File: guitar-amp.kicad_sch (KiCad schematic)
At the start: 4 parts, among them J1 AudioJack2_SwitchT, U1 ECC81, U2 ECC81, U3 EL84

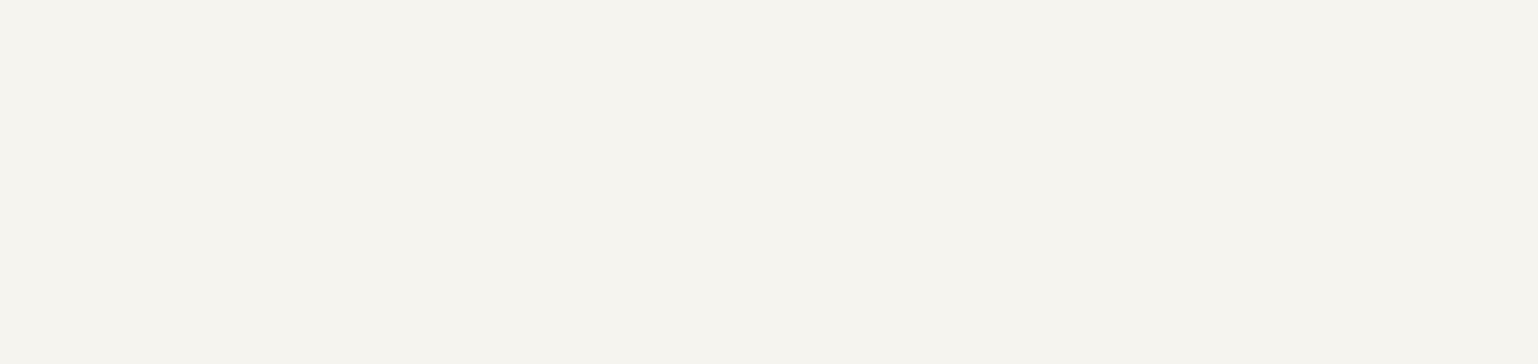
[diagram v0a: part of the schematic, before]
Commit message: Add resistors
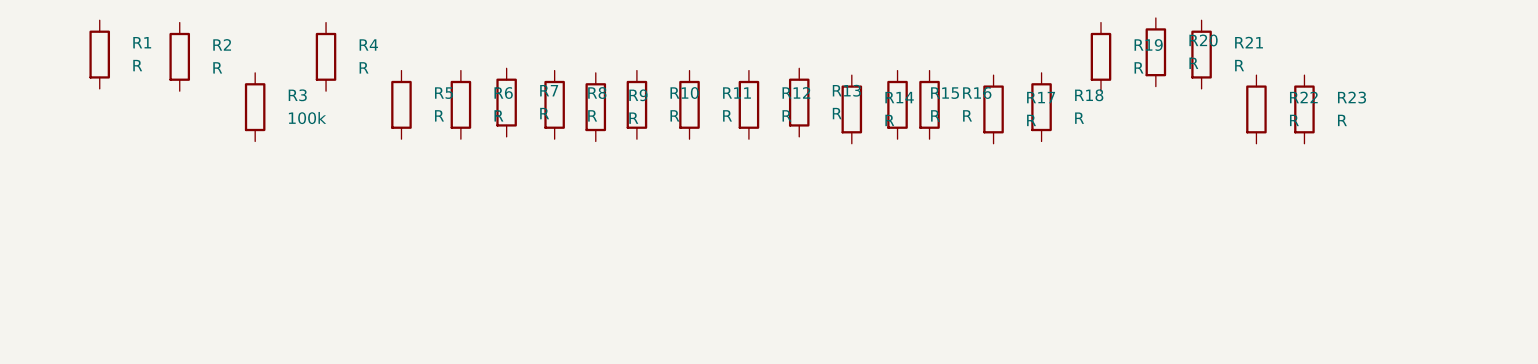
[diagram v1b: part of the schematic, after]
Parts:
- added R1, R19, R2, R20, R21, R4: R, Resistor_THT:R_Axial_DIN0411_L9.9mm_D3.6mm_P12.70mm_Horizontal, symbol Device:R
- added R10, R11, R12, R13, R14, R15, R16, R17, R18, R22, R23, R5, R6, R7, R8, R9: R, Resistor_THT:R_Axial_DIN0207_L6.3mm_D2.5mm_P7.62mm_Horizontal, symbol Device:R
- added R3: 100k, Resistor_THT:R_Axial_DIN0207_L6.3mm_D2.5mm_P7.62mm_Horizontal, symbol Device:R

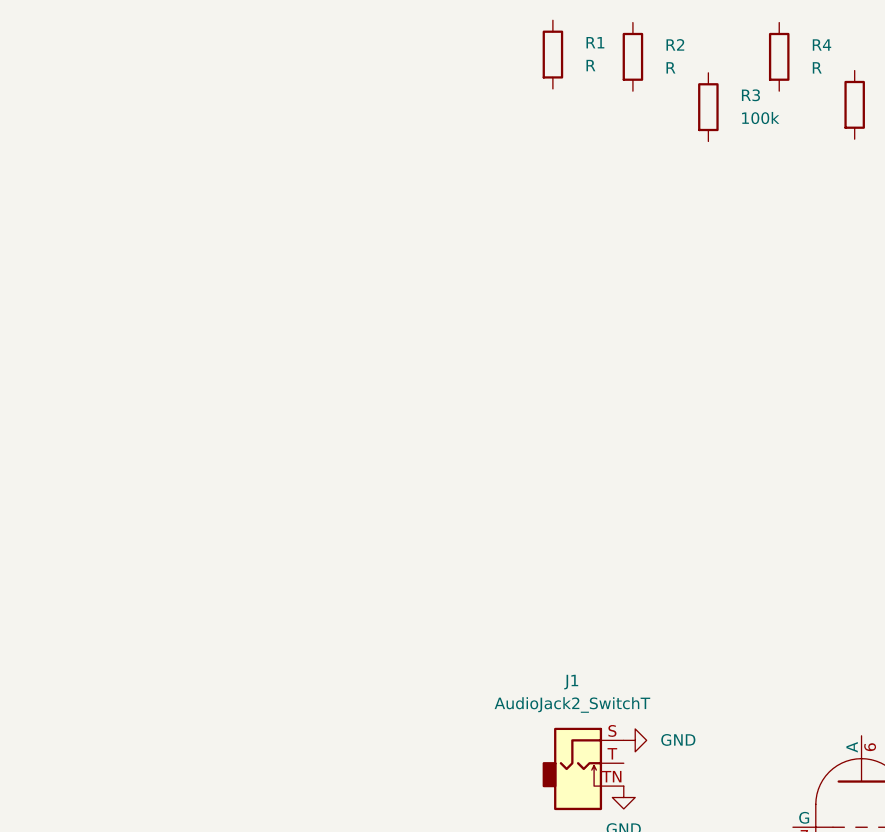
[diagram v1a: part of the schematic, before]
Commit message: Add capacitors
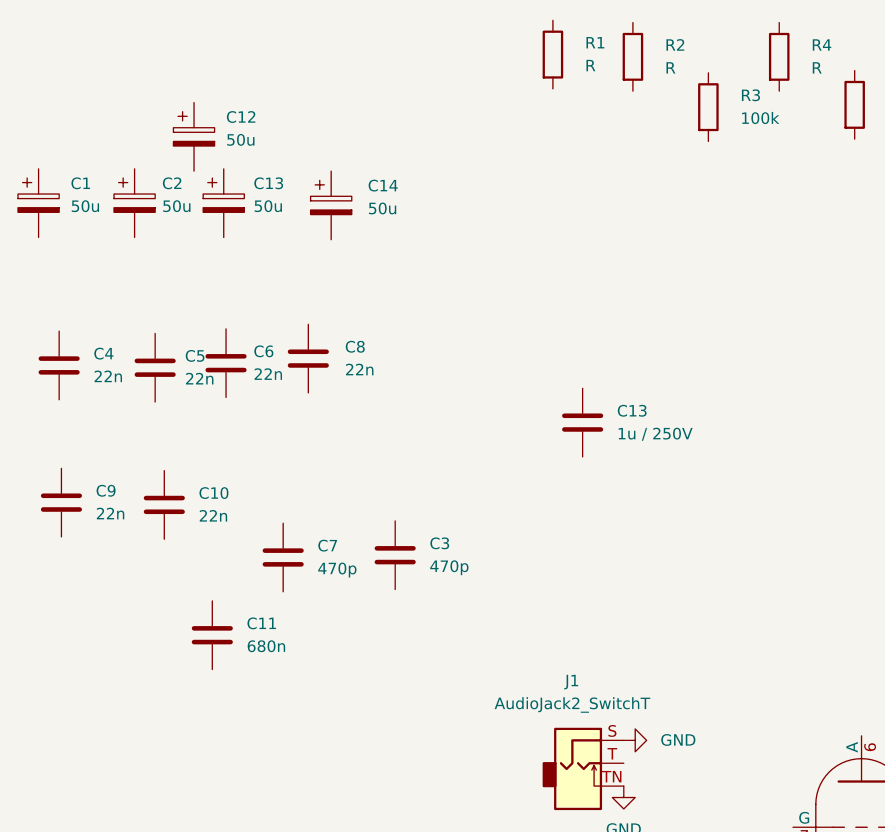
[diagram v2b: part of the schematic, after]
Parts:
- added C1, C13, C14, C2: 50u, Capacitor_THT:CP_Radial_D16.0mm_P7.50mm, symbol Device:C_Polarized
- added C10, C9: 22n, Capacitor_THT:C_Rect_L10.3mm_W5.0mm_P7.50mm_MKS4, symbol Device:C
- added C11: 680n, Capacitor_THT:C_Axial_L17.0mm_D7.0mm_P20.00mm_Horizontal, symbol Device:C
- added C12: 50u, Capacitor_THT:CP_Radial_D6.3mm_P2.50mm, symbol Device:C_Polarized
- added C13: 1u / 250V, Capacitor_THT:C_Rect_L27.0mm_W9.0mm_P23.00mm, symbol Device:C
- added C3, C7: 470p, Capacitor_THT:C_Disc_D7.0mm_W2.5mm_P5.00mm, symbol Device:C
- added C4, C5, C6, C8: 22n, Capacitor_THT:C_Rect_L18.0mm_W5.0mm_P15.00mm_FKS3_FKP3, symbol Device:C

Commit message: Add potentiometers
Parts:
- added VR3: 220k LIN, Potentiometer_THT:Potentiometer_Alps_RK163_Single_Horizontal, symbol Device:R_Potentiometer
- added VR5: 25k LIN, Potentiometer_THT:Potentiometer_Alps_RK163_Single_Horizontal, symbol Device:R_Potentiometer
- renumbered C13 to C15
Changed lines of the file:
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@@
     (pin "2")
+  )
+  (symbol (lib_id "Device:R_Potentiometer") (at -19.558 115.57 180) (unit 1)
+    (in_bom yes) (on_board yes) (fields_autoplaced)
+    (property "Reference" "VR5" (id 0) (at -17.78 114.2999 0)
+      (effects (font (size 1.27 1.27)) (justify right))
+    )
+    (property "Value" "25k LIN" (id 1) (at -17.78 116.8399 0)
+      (effects (font (size 1.27 1.27)) (justify right))
+    )
+    (property "Footprint" "Potentiometer_THT:Potentiometer_Alps_RK163_Single_Horizontal" (id 2) (at -19.558 115.57 0)
+      (effects (font (size 1.27 1.27)) hide)
+    )
+    (property "Datasheet" "~" (id 3) (at -19.558 115.57 0)
+      (effects (font (size 1.27 1.27)) hide)
+    )
+    (pin "1")
+    (pin "2")
+    (pin "3")
   )
   (symbol (lib_id "Device:R") (at 103.886 25.4 0) (unit 1)
@@
   (symbol (lib_id "Device:C") (at 23.622 60.198 0) (unit 1)
     (in_bom yes) (on_board yes) (fields_autoplaced)
-    (property "Reference" "C13" (id 0) (at 27.432 58.9279 0)
+    (property "Reference" "C15" (id 0) (at 27.432 58.9279 0)
       (effects (font (size 1.27 1.27)) (justify left))
     )
@@
     (pin "2")
   )
+  (symbol (lib_id "Device:R_Potentiometer") (at -39.624 115.316 180) (unit 1)
+    (in_bom yes) (on_board yes) (fields_autoplaced)
+    (property "Reference" "VR3" (id 0) (at -35.56 114.0459 0)
+      (effects (font (size 1.27 1.27)) (justify right))
+    )
+    (property "Value" "220k LIN" (id 1) (at -35.56 116.5859 0)
+      (effects (font (size 1.27 1.27)) (justify right))
+    )
+    (property "Footprint" "Potentiometer_THT:Potentiometer_Alps_RK163_Single_Horizontal" (id 2) (at -39.624 115.316 0)
+      (effects (font (size 1.27 1.27)) hide)
+    )
+    (property "Datasheet" "~" (id 3) (at -39.624 115.316 0)
+      (effects (font (size 1.27 1.27)) hide)
+    )
+    (pin "1")
+    (pin "2")
+    (pin "3")
+  )
   (symbol (lib_id "Device:C") (at -9.652 75.184 0) (unit 1)
     (in_bom yes) (on_board yes) (fields_autoplaced)
@@
       (reference "C12") (unit 1) (value "50u") (footprint "Capacitor_THT:CP_Radial_D6.3mm_P2.50mm")
     )
-    (path "/b375741c-d524-4718-8b51-0b70caa17dd3"
-      (reference "C13") (unit 1) (value "1u / 250V") (footprint "Capacitor_THT:C_Rect_L27.0mm_W9.0mm_P23.00mm")
-    )
     (path "/b75fbf3a-5bd9-43fd-b230-2ee6aeb56be1"
       (reference "C13") (unit 1) (value "50u") (footprint "Capacitor_THT:CP_Radial_D16.0mm_P7.50mm")
@@
       (reference "C14") (unit 1) (value "50u") (footprint "Capacitor_THT:CP_Radial_D16.0mm_P7.50mm")
     )
+    (path "/b375741c-d524-4718-8b51-0b70caa17dd3"
+      (reference "C15") (unit 1) (value "1u / 250V") (footprint "Capacitor_THT:C_Rect_L27.0mm_W9.0mm_P23.00mm")
+    )
     (path "/2ecf6c5f-4a2c-4138-91f3-65fe29bb0d89"
       (reference "J1") (unit 1) (value "AudioJack2_SwitchT") (footprint "")
@@
       (reference "U3") (unit 2) (value "EL84") (footprint "Valve:Valve_Noval_P")
     )
-  )
+    (path "/f278ad10-0794-4c12-86f7-ca40b6dacbad"
+      (reference "VR3") (unit 1) (value "220k LIN") (footprint "Potentiometer_THT:Potentiometer_Alps_RK163_Single_Horizontal")
+    )
+    (path "/4d46036e-99cb-4181-bcbd-a7e7c6a227c4"
+      (reference "VR5") (unit 1) (value "25k LIN") (footprint "Potentiometer_THT:Potentiometer_Alps_RK163_Single_Horizontal")
+    )
+  )

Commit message: Add guitar jack
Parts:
- removed J1: AudioJack2_SwitchT, symbol Connector:AudioJack2_SwitchT
- added J?: AudioJack3_Switch, Connector_Audio:Jack_6.35mm_Neutrik_NMJ6HFD2-AU_Horizontal, symbol Connector:AudioJack3_Switch
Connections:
- net GND: now also J?.S, J?.SN
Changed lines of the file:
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@@
     (pin "9")
   )
-  (symbol (lib_id "power:GND") (at 28.194 100.584 0) (unit 1)
-    (in_bom yes) (on_board yes) (fields_autoplaced)
-    (property "Reference" "#PWR0101" (id 0) (at 28.194 106.934 0)
-      (effects (font (size 1.27 1.27)) hide)
-    )
-    (property "Value" "GND" (id 1) (at 28.194 105.41 0))
-    (property "Footprint" "" (id 2) (at 28.194 100.584 0)
-      (effects (font (size 1.27 1.27)) hide)
-    )
-    (property "Datasheet" "" (id 3) (at 28.194 100.584 0)
-      (effects (font (size 1.27 1.27)) hide)
-    )
-    (pin "1")
-  )
   (symbol (lib_id "Device:R") (at 29.21 19.558 0) (unit 1)
     (in_bom yes) (on_board yes) (fields_autoplaced)
@@
     (pin "1")
     (pin "2")
-  )
-  (symbol (lib_id "power:GND") (at 28.194 95.504 90) (unit 1)
-    (in_bom yes) (on_board yes) (fields_autoplaced)
-    (property "Reference" "#PWR0102" (id 0) (at 34.544 95.504 0)
-      (effects (font (size 1.27 1.27)) hide)
-    )
-    (property "Value" "GND" (id 1) (at 32.258 95.5039 90)
-      (effects (font (size 1.27 1.27)) (justify right))
-    )
-    (property "Footprint" "" (id 2) (at 28.194 95.504 0)
-      (effects (font (size 1.27 1.27)) hide)
-    )
-    (property "Datasheet" "" (id 3) (at 28.194 95.504 0)
-      (effects (font (size 1.27 1.27)) hide)
-    )
-    (pin "1")
-  )
-  (symbol (lib_id "Connector:AudioJack2_SwitchT") (at 23.114 98.044 0) (unit 1)
-    (in_bom yes) (on_board yes) (fields_autoplaced)
-    (property "Reference" "J1" (id 0) (at 22.479 88.9 0))
-    (property "Value" "AudioJack2_SwitchT" (id 1) (at 22.479 91.44 0))
-    (property "Footprint" "" (id 2) (at 23.114 98.044 0)
-      (effects (font (size 1.27 1.27)) hide)
-    )
-    (property "Datasheet" "~" (id 3) (at 23.114 98.044 0)
-      (effects (font (size 1.27 1.27)) hide)
-    )
-    (pin "S")
-    (pin "T")
-    (pin "TN")
   )
   (symbol (lib_id "Valve:ECC81") (at 54.61 105.156 0) (unit 1)
@@
     (pin "5")
     (pin "9")
+  )
+  (symbol (lib_id "Connector:AudioJack3_Switch") (at 25.908 127.762 0) (unit 1)
+    (in_bom yes) (on_board yes) (fields_autoplaced)
+    (property "Reference" "J?" (id 0) (at 24.003 115.824 0))
+    (property "Value" "AudioJack3_Switch" (id 1) (at 24.003 118.364 0))
+    (property "Footprint" "Connector_Audio:Jack_6.35mm_Neutrik_NMJ6HFD2-AU_Horizontal" (id 2) (at 25.908 127.762 0)
+      (effects (font (size 1.27 1.27)) hide)
+    )
+    (property "Datasheet" "~" (id 3) (at 25.908 127.762 0)
+      (effects (font (size 1.27 1.27)) hide)
+    )
+    (pin "R")
+    (pin "RN")
+    (pin "S")
+    (pin "SN")
+    (pin "T")
+    (pin "TN")
   )
   (symbol (lib_id "Device:R") (at 75.438 25.146 0) (unit 1)
@@
     (pin "2")
   )
+  (symbol (lib_id "power:GND") (at 30.988 125.222 90) (unit 1)
+    (in_bom yes) (on_board yes) (fields_autoplaced)
+    (property "Reference" "#PWR?" (id 0) (at 37.338 125.222 0)
+      (effects (font (size 1.27 1.27)) hide)
+    )
+    (property "Value" "GND" (id 1) (at 34.544 125.2219 90)
+      (effects (font (size 1.27 1.27)) (justify right))
+    )
+    (property "Footprint" "" (id 2) (at 30.988 125.222 0)
+      (effects (font (size 1.27 1.27)) hide)
+    )
+    (property "Datasheet" "" (id 3) (at 30.988 125.222 0)
+      (effects (font (size 1.27 1.27)) hide)
+    )
+    (pin "1")
+  )
   (symbol (lib_id "Device:R") (at 124.968 25.146 0) (unit 1)
     (in_bom yes) (on_board yes) (fields_autoplaced)
@@
     (pin "2")
   )
+  (symbol (lib_id "power:GND") (at 30.988 122.682 90) (unit 1)
+    (in_bom yes) (on_board yes) (fields_autoplaced)
+    (property "Reference" "#PWR?" (id 0) (at 37.338 122.682 0)
+      (effects (font (size 1.27 1.27)) hide)
+    )
+    (property "Value" "GND" (id 1) (at 34.544 122.6819 90)
+      (effects (font (size 1.27 1.27)) (justify right))
+    )
+    (property "Footprint" "" (id 2) (at 30.988 122.682 0)
+      (effects (font (size 1.27 1.27)) hide)
+    )
+    (property "Datasheet" "" (id 3) (at 30.988 122.682 0)
+      (effects (font (size 1.27 1.27)) hide)
+    )
+    (pin "1")
+  )
   (symbol (lib_id "Device:R") (at 45.466 19.558 0) (unit 1)
     (in_bom yes) (on_board yes) (fields_autoplaced)
@@
   )
   (symbol_instances
-    (path "/138d8c5c-02de-4f8a-a7a7-ab72cf53367f"
-      (reference "#PWR0101") (unit 1) (value "GND") (footprint "")
-    )
-    (path "/292ff299-5d7c-4749-8741-8cede0f0c0fb"
-      (reference "#PWR0102") (unit 1) (value "GND") (footprint "")
+    (path "/6a774d59-6df9-40fb-b71c-c30cd6406089"
+      (reference "#PWR?") (unit 1) (value "GND") (footprint "")
+    )
+    (path "/e6fe2549-38b0-40df-8f82-6361f508ea82"
+      (reference "#PWR?") (unit 1) (value "GND") (footprint "")
     )
     (path "/a5a1e963-dbc6-4646-bdde-fe8576b73b7d"
@@
       (reference "C15") (unit 1) (value "1u / 250V") (footprint "Capacitor_THT:C_Rect_L27.0mm_W9.0mm_P23.00mm")
     )
-    (path "/2ecf6c5f-4a2c-4138-91f3-65fe29bb0d89"
-      (reference "J1") (unit 1) (value "AudioJack2_SwitchT") (footprint "")
+    (path "/3a4fbf03-7074-4eaf-a2b2-47087d84353c"
+      (reference "J?") (unit 1) (value "AudioJack3_Switch") (footprint "Connector_Audio:Jack_6.35mm_Neutrik_NMJ6HFD2-AU_Horizontal")
     )
     (path "/eb0eca1a-a845-4c07-9c98-8a80d6f813f5"

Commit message: Model the schematic
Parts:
- added D1: Bridge Rectifier, Diode_THT:Diode_Bridge_32.0x5.6x17.0mm_P10.0mm_P7.5mm, symbol Diode_Bridge:B40C3x00-2200A
- added F1: Fuse, Fuse:Fuseholder_Cylinder-5x20mm_Schurter_0031_8201_Horizontal_Open, symbol Device:Fuse
- added J1: Speaker Output, TerminalBlock_Phoenix:TerminalBlock_Phoenix_MKDS-1,5-2-5.08_1x02_P5.08mm_Horizontal, symbol Connector:AudioJack2_SwitchT
- added J3: AC Mains, symbol Connector:Screw_Terminal_01x03
- added S3: SW_Push_DPDT, Button_Switch_THT:SW_CuK_JS202011CQN_DPDT_Straight, symbol Switch:SW_Push_DPDT
- added T1: 5W OT, symbol Device:Transformer_1P_1S_SO8
- added T2: Transformer_1P_2S, symbol Device:Transformer_1P_2S
- added VR1, VR2, VR6: 1M, Potentiometer_THT:Potentiometer_Piher_PT-15-V15_Vertical, symbol Device:R_Potentiometer
- added VR4: 1M Log, Potentiometer_THT:Potentiometer_Piher_PT-15-V15_Vertical, symbol Device:R_Potentiometer
- C10, C9: value 22n -> 1u
- C12: value 50u -> 100u / 25V
- J2: renamed from J?; value AudioJack3_Switch -> Input
- R1: value R -> 10k
- R10: value R -> 68k
- R11, R12, R15, R17: value R -> 470k
- R13: value R -> 1M
- R14: value R -> 2.7k
- R16: value R -> 1.2k
- R18: value R -> 820
- R19: value R -> 130
- R2, R4: value R -> 1k
- R20: value R -> 100 / 2W
- R21, R5, R6, R7: value R -> 100k
- R22, R23: value R -> 100
- R8: value R -> 33k
- R9: value R -> 5.6k
- renumbered U1 to V1, U2 to V2, U3 to V3
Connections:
- net GND is gone; now on net Earth: J2.S, J2.SN
- net at C9.1: now also R16.1, V1.3 (K)
- net Earth: now reaches C9.2
- net Earth: now also C1.2, C10.2, C11.2, C12.2, C13.2, C14.2, C2.2, J2.RN, J2.TN, R13.2, R14.2, R15.2, R16.2, R17.2, R18.2, R19.2, R21.1, R7.2, VR5.1, D1.1 (-), J1.S, J3.2 (Pin_2), T1.5 (SA), VR1.3, VR2.3, VR6.3
- net at V1.1 (A): now also C5.1
- net at V1.2 (G): now also C7.2, R11.2, R15.1
- net at R2.1: now also C2.1, R1.2, R3.1, R4.1, V2.1 (A)
- net at R2.2: now also C14.1, R20.2, R21.2, T1.4 (AB)
- net at R10.1: now also J2.T, R13.1
- net at R10.2: now also C15.1
- net at C4.1: now also R5.2, V1.6 (A)
- net at C4.2: now also VR1.1
- net at C11.1: now also R14.1, V1.8 (K)
- net at R17.1: now also R12.2, V2.7 (G)
- net at V1.7 (G): now also C15.2
- net at R9.1: now also V3.2 (G1)
- net at R9.2: now also VR6.2
- net at V3.4 (F1): now also R22.2, V1.4 (F1), V1.5 (F1), V2.4 (F1), V2.5 (F1), T2.5 (SC)
- net at V3.5 (F2): now also R23.2, V1.9 (F2), V2.9 (F2), T2.6 (SD)
- net at R8.1: now also C3.1, R7.1, V2.3 (K)
- net at R8.2: now also C6.1, C8.1
- net at VR5.2: now also C8.2
- net at VR5.3: now also VR4.3
- net at C10.1: now also R18.1, V2.8 (K)
- net at V2.2 (G): now also R3.2, V2.6 (A)
- net at R20.1: now also C13.1, D1.4 (+)
- net at C5.2: now also R6.2, VR2.1
- net at R22.1: now also C12.1, R19.1, R23.1, V3.3 (K_G3)
- net at R6.1: now also C1.1, R1.1, R5.1
- net at R12.1: now also VR2.2
- net at V3.7 (A): now also T1.1 (AA)
- net at V3.9 (G2): now also R4.2
- net at C3.2: now also VR3.3
- net at R11.1: now also C7.1, VR1.2
- net at C6.2: now also VR3.1, VR4.2
- net at VR3.2: now also VR6.1
- new net: D1.2, T2.3 (SA)
- new net: D1.3, T2.4 (SB)
- new net: J1.T, T1.8 (SB)
- new net: F1.1, J3.1 (Pin_1)
- new net: F1.2, S3.1 (A)
- new net: S3.2 (B), T2.1 (AA)
- new net: S3.5 (B), T2.2 (AB)
- new net: J3.3 (Pin_3), S3.4 (A)
- no-connect marks 0 -> 5
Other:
- note added: "0VDC"
- note added: "143VDC"
- note added: "227VDC"
- note added: "241VDC"
- note added: "810mVDC"
- note added: "960mVDC"
- note added: "Bass"
- note added: "Cathode follower"
- note added: "Filament Reference / Hum Reduction Resistors"
- note added: "GAIN1"
- note added: "GAIN2"
- note added: "Kein Elko?"
- note added: "Middle"
- note added: "PREAMP STAGE 1"
- note added: "PREAMP STAGE 2"
- note added: "PREAMP STAGE 3"
- note added: "Supply Decoupling Filter"
- note added: "TODO: Which Bridge Rectifier??"
- note added: "Tone Control"
- note added: "Treble"
- note added: "Why 250V"
- moved on the sheet: C1, C10, C11, C12, C13, C14, C15, C2, C3, C4, C5, C6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
